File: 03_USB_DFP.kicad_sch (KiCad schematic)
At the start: 0 parts

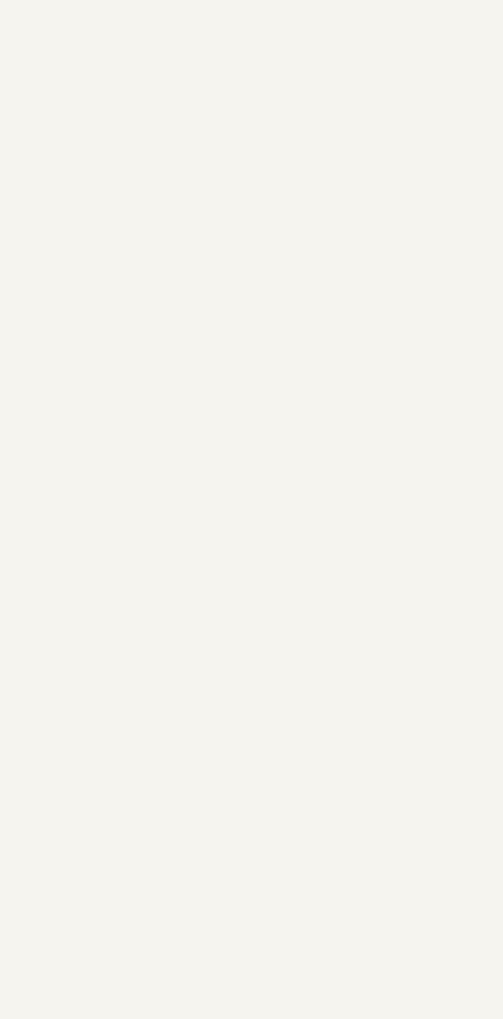
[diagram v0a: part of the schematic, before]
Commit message: add usb hub controller schematic, fix up redriver
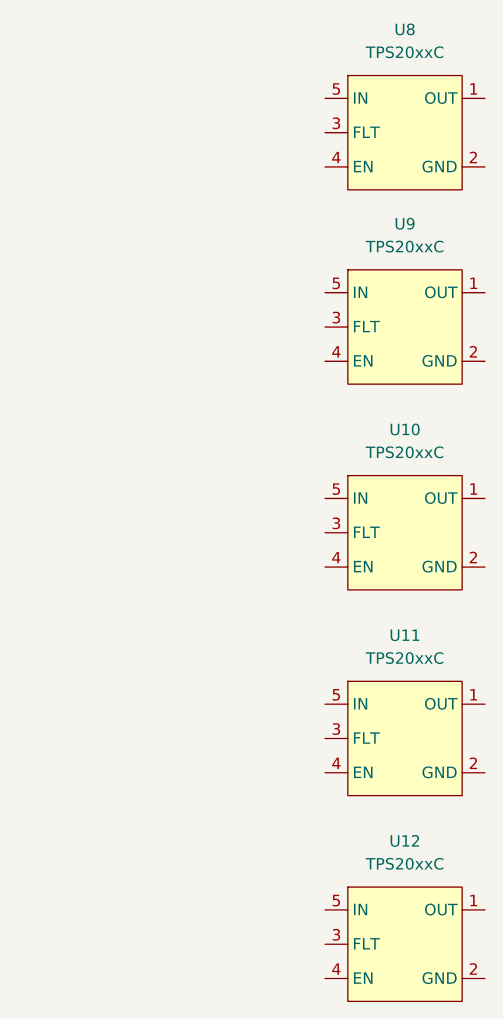
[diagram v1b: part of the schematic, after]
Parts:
- added U10, U11, U12, U8, U9: TPS20xxC, Package_TO_SOT_SMD:SOT-23-5, symbol CakeUSB:TPS20xxC
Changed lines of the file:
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@@
     (effects (font (size 1.27 1.27)) (justify left bottom))
   )
+  (symbol (lib_id "CakeUSB:TPS20xxC") (at 181.61 133.35 0) (unit 1)
+    (in_bom yes) (on_board yes) (dnp no) (fields_autoplaced)
+    (property "Reference" "U12" (at 181.61 121.92 0)
+      (effects (font (size 1.27 1.27)))
+    )
+    (property "Value" "TPS20xxC" (at 181.61 124.46 0)
+      (effects (font (size 1.27 1.27)))
+    )
+    (property "Footprint" "Package_TO_SOT_SMD:SOT-23-5" (at 203.2 114.3 0)
+      (effects (font (size 1.27 1.27)) hide)
+    )
+    (property "Datasheet" "https://www.ti.com/lit/ds/symlink/tps2001c.pdf" (at 212.09 116.84 0)
+      (effects (font (size 1.27 1.27)) hide)
+    )
+    (pin "1")
+    (pin "5")
+    (pin "2")
+    (pin "3")
+    (pin "4")
+    (instances
+      (project "USBHUB"
+        (path "/d5edc647-9ac3-4ac1-ab8a-57c77be3f4d3/aef239ad-726b-4cbb-b085-3b57a4599b3b"
+          (reference "U12") (unit 1)
+        )
+      )
+    )
+  )
+  (symbol (lib_id "CakeUSB:TPS20xxC") (at 181.61 87.63 0) (unit 1)
+    (in_bom yes) (on_board yes) (dnp no) (fields_autoplaced)
+    (property "Reference" "U10" (at 181.61 76.2 0)
+      (effects (font (size 1.27 1.27)))
+    )
+    (property "Value" "TPS20xxC" (at 181.61 78.74 0)
+      (effects (font (size 1.27 1.27)))
+    )
+    (property "Footprint" "Package_TO_SOT_SMD:SOT-23-5" (at 203.2 68.58 0)
+      (effects (font (size 1.27 1.27)) hide)
+    )
+    (property "Datasheet" "https://www.ti.com/lit/ds/symlink/tps2001c.pdf" (at 212.09 71.12 0)
+      (effects (font (size 1.27 1.27)) hide)
+    )
+    (pin "1")
+    (pin "5")
+    (pin "2")
+    (pin "3")
+    (pin "4")
+    (instances
+      (project "USBHUB"
+        (path "/d5edc647-9ac3-4ac1-ab8a-57c77be3f4d3/aef239ad-726b-4cbb-b085-3b57a4599b3b"
+          (reference "U10") (unit 1)
+        )
+      )
+    )
+  )
+  (symbol (lib_id "CakeUSB:TPS20xxC") (at 181.61 43.18 0) (unit 1)
+    (in_bom yes) (on_board yes) (dnp no) (fields_autoplaced)
+    (property "Reference" "U8" (at 181.61 31.75 0)
+      (effects (font (size 1.27 1.27)))
+    )
+    (property "Value" "TPS20xxC" (at 181.61 34.29 0)
+      (effects (font (size 1.27 1.27)))
+    )
+    (property "Footprint" "Package_TO_SOT_SMD:SOT-23-5" (at 203.2 24.13 0)
+      (effects (font (size 1.27 1.27)) hide)
+    )
+    (property "Datasheet" "https://www.ti.com/lit/ds/symlink/tps2001c.pdf" (at 212.09 26.67 0)
+      (effects (font (size 1.27 1.27)) hide)
+    )
+    (pin "1")
+    (pin "5")
+    (pin "2")
+    (pin "3")
+    (pin "4")
+    (instances
+      (project "USBHUB"
+        (path "/d5edc647-9ac3-4ac1-ab8a-57c77be3f4d3/aef239ad-726b-4cbb-b085-3b57a4599b3b"
+          (reference "U8") (unit 1)
+        )
+      )
+    )
+  )
+  (symbol (lib_id "CakeUSB:TPS20xxC") (at 181.61 64.77 0) (unit 1)
+    (in_bom yes) (on_board yes) (dnp no) (fields_autoplaced)
+    (property "Reference" "U9" (at 181.61 53.34 0)
+      (effects (font (size 1.27 1.27)))
+    )
+    (property "Value" "TPS20xxC" (at 181.61 55.88 0)
+      (effects (font (size 1.27 1.27)))
+    )
+    (property "Footprint" "Package_TO_SOT_SMD:SOT-23-5" (at 203.2 45.72 0)
+      (effects (font (size 1.27 1.27)) hide)
+    )
+    (property "Datasheet" "https://www.ti.com/lit/ds/symlink/tps2001c.pdf" (at 212.09 48.26 0)
+      (effects (font (size 1.27 1.27)) hide)
+    )
+    (pin "1")
+    (pin "5")
+    (pin "2")
+    (pin "3")
+    (pin "4")
+    (instances
+      (project "USBHUB"
+        (path "/d5edc647-9ac3-4ac1-ab8a-57c77be3f4d3/aef239ad-726b-4cbb-b085-3b57a4599b3b"
+          (reference "U9") (unit 1)
+        )
+      )
+    )
+  )
+  (symbol (lib_id "CakeUSB:TPS20xxC") (at 181.61 110.49 0) (unit 1)
+    (in_bom yes) (on_board yes) (dnp no) (fields_autoplaced)
+    (property "Reference" "U11" (at 181.61 99.06 0)
+      (effects (font (size 1.27 1.27)))
+    )
+    (property "Value" "TPS20xxC" (at 181.61 101.6 0)
+      (effects (font (size 1.27 1.27)))
+    )
+    (property "Footprint" "Package_TO_SOT_SMD:SOT-23-5" (at 203.2 91.44 0)
+      (effects (font (size 1.27 1.27)) hide)
+    )
+    (property "Datasheet" "https://www.ti.com/lit/ds/symlink/tps2001c.pdf" (at 212.09 93.98 0)
+      (effects (font (size 1.27 1.27)) hide)
+    )
+    (pin "1")
+    (pin "5")
+    (pin "2")
+    (pin "3")
+    (pin "4")
+    (instances
+      (project "USBHUB"
+        (path "/d5edc647-9ac3-4ac1-ab8a-57c77be3f4d3/aef239ad-726b-4cbb-b085-3b57a4599b3b"
+          (reference "U11") (unit 1)
+        )
+      )
+    )
+  )
 )

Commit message: WIP hub and DFP
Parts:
- added D12, D13, D14, D15, D16, D17, D18, D19, D20, D21, D22, D23: ESD122DMx, Cake_USB:ESD122DMX, symbol CakeUSB:ESD122DMx
- added U14, U15, U16, U17: USB_3_Type_A_Molex_484080003, Cake_USB:Molex_484080003, symbol CakeUSB:USB_3_Type_A_Molex_484080003
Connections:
- new net GND: D12.1 (GND), D13.1 (GND), D14.1 (GND), D15.1 (GND), D16.1 (GND), D17.1 (GND), D18.1 (GND), D19.1 (GND), D20.1 (GND), D21.1 (GND), D22.1 (GND), D23.1 (GND), U14.4 (GND), U14.7 (DRAIN), U15.4 (GND), U15.7 (DRAIN), U16.4 (GND), U16.7 (DRAIN), U17.4 (GND), U17.7 (DRAIN)
- new net HUB1_DS1_DM: D14.3 (IO2), U14.2 (D-)
- new net HUB1_DS1_DP: D14.2 (IO1), U14.3 (D+)
- new net HUB1_DS1_RXM: D13.3 (IO2), U14.5 (SSRX-)
- new net HUB1_DS1_RXP: D13.2 (IO1), U14.6 (SSRX+)
- new net HUB1_DS1_TXM: D12.3 (IO2), U14.8 (SSTX-)
- new net HUB1_DS1_TXP: D12.2 (IO1), U14.9 (SSTX+)
- new net HUB1_DS2_DM: D17.3 (IO2), U15.2 (D-)
- new net HUB1_DS2_DP: D17.2 (IO1), U15.3 (D+)
- new net HUB1_DS2_RXM: D16.3 (IO2), U15.5 (SSRX-)
- new net HUB1_DS2_RXP: D16.2 (IO1), U15.6 (SSRX+)
- new net HUB1_DS2_TXM: D15.3 (IO2), U15.8 (SSTX-)
- new net HUB1_DS2_TXP: D15.2 (IO1), U15.9 (SSTX+)
- new net HUB1_DS3_DM: D20.3 (IO2), U16.2 (D-)
- new net HUB1_DS3_DP: D20.2 (IO1), U16.3 (D+)
- new net HUB1_DS3_RXM: D19.3 (IO2), U16.5 (SSRX-)
- new net HUB1_DS3_RXP: D19.2 (IO1), U16.6 (SSRX+)
- new net HUB1_DS3_TXM: D18.3 (IO2), U16.8 (SSTX-)
- new net HUB1_DS3_TXP: D18.2 (IO1), U16.9 (SSTX+)
- new net HUB1_DS4_DM: D23.3 (IO2), U17.2 (D-)
- new net HUB1_DS4_DP: D23.2 (IO1), U17.3 (D+)
- new net HUB1_DS4_RXM: D22.3 (IO2), U17.5 (SSRX-)
- new net HUB1_DS4_RXP: D22.2 (IO1), U17.6 (SSRX+)
- new net HUB1_DS4_TXM: D21.3 (IO2), U17.8 (SSTX-)
- new net HUB1_DS4_TXP: D21.2 (IO1), U17.9 (SSTX+)
- new net USB_DS1_VBUS: U14.1 (VBUS)
- new net USB_DS2_VBUS: U15.1 (VBUS)
- new net USB_DS3_VBUS: U16.1 (VBUS)
- new net USB_DS4_VBUS: U17.1 (VBUS)
- no-connect marks 0 -> 8
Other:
- note removed: "Each output port must have ESD + power switch TPS2001C e.g."
- moved on the sheet: U10, U11, U12, U8, U9

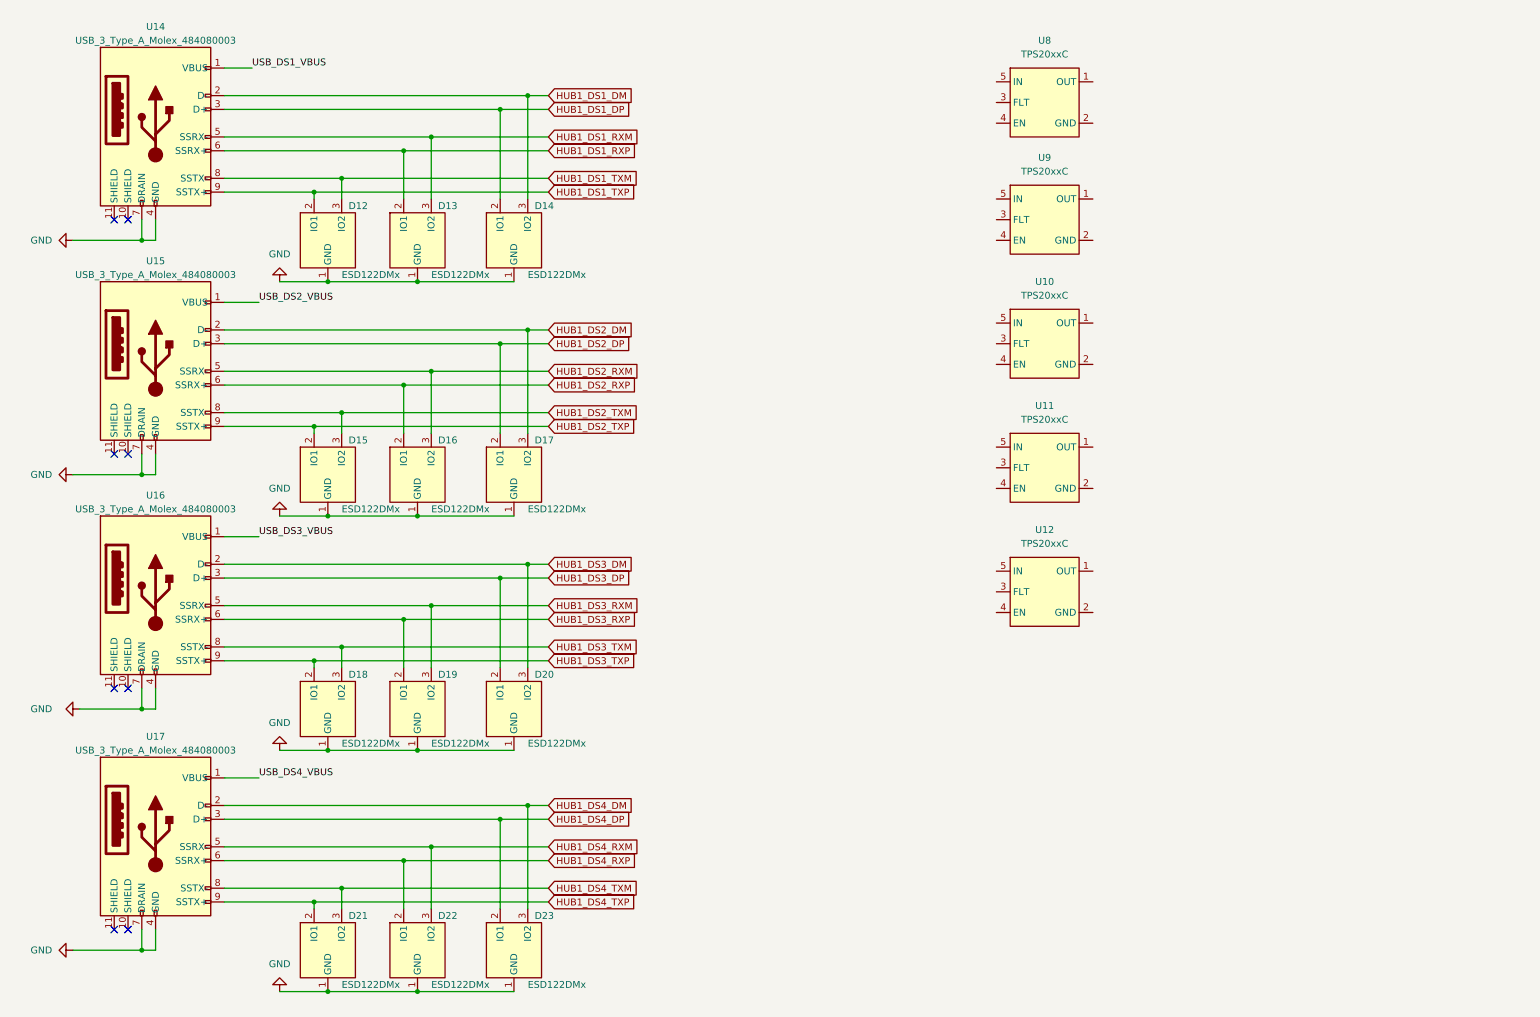
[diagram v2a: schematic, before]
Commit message: finish up schematics and ERC
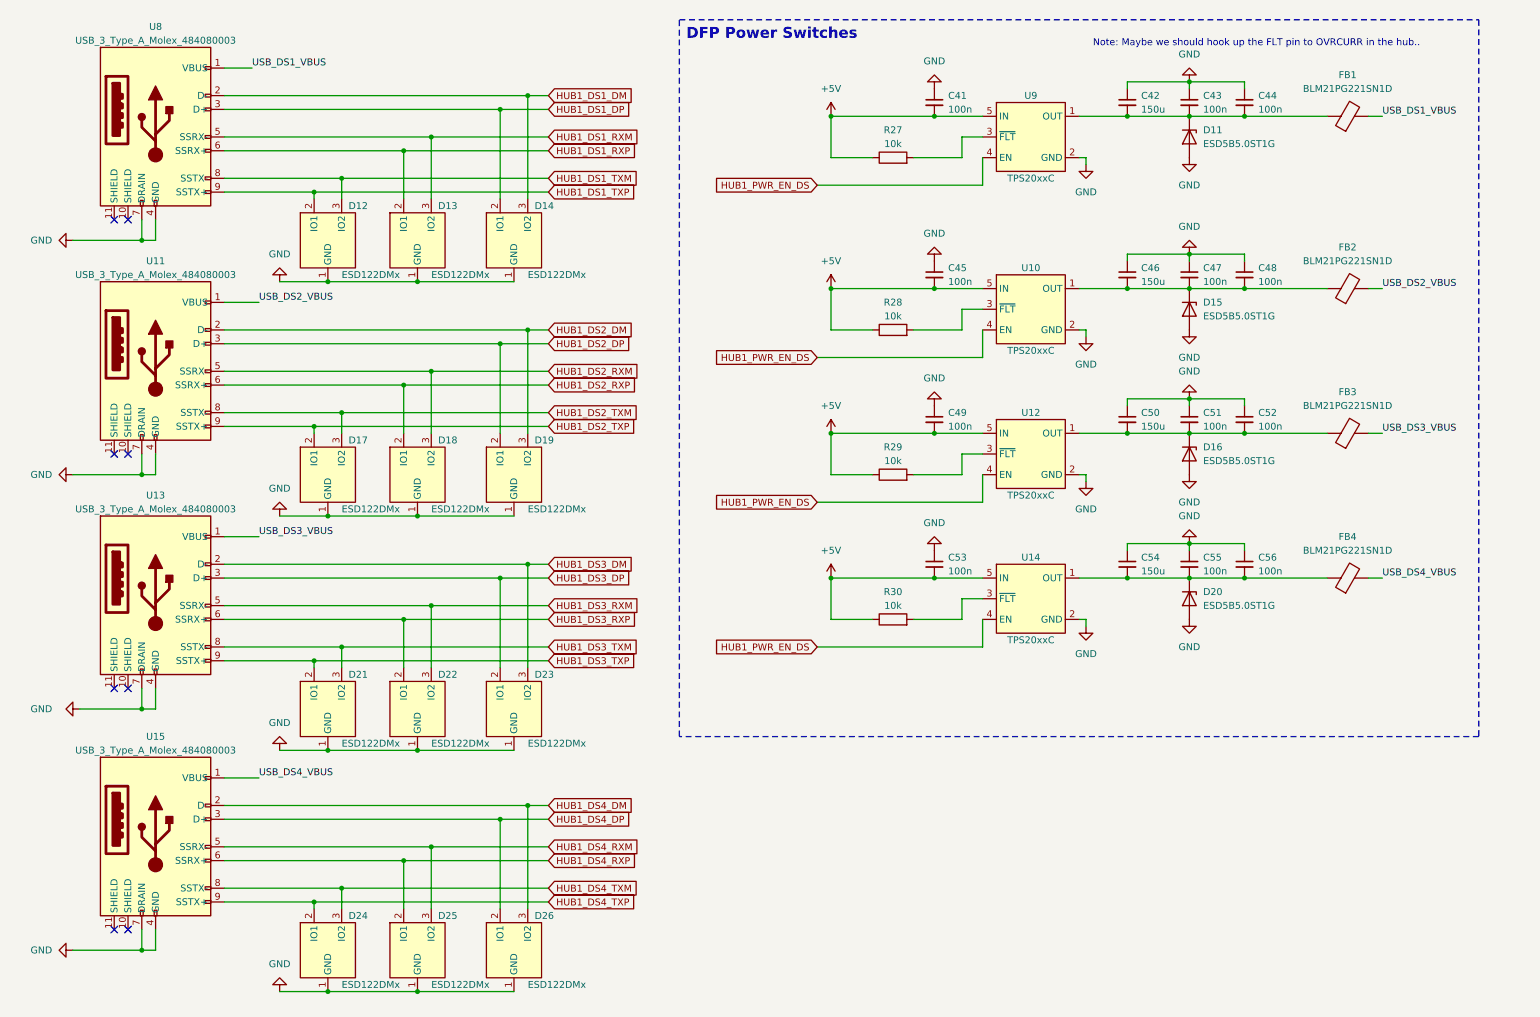
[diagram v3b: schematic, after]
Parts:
- removed U11, U9: TPS20xxC, Package_TO_SOT_SMD:SOT-23-5, symbol CakeUSB:TPS20xxC
- added C41, C43, C44, C45, C47, C48, C49, C51, C52, C53, C55, C56: 100n, symbol Device:C_Small
- added C42, C46, C50, C54: 150u, symbol Device:C_Small
- added D11, D15, D16, D20: ESD5B5.0ST1G, symbol Device:D_Zener
- added FB1, FB2, FB3, FB4: BLM21PG221SN1D, symbol Device:FerriteBead
- added R27, R28, R29, R30: 10k, symbol Device:R
- added U14: TPS20xxC, Package_TO_SOT_SMD:SOT-23-5, symbol CakeUSB:TPS20xxC
- renumbered D15 to D17, D16 to D18, D17 to D19, D18 to D21, D19 to D22, D20 to D23, D21 to D24, D22 to D25, D23 to D26, U15 to U11, U16 to U13, U17 to U15, U14 to U8, U8 to U9
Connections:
- net GND: now also U10.2 (GND), U12.2 (GND), U9.2 (GND), C41.1, C42.1, C43.1, C44.1, C45.1, C46.1, C47.1, C48.1, C49.1, C50.1, C51.1, C52.1, C53.1, C54.1, C55.1, C56.1, D11.2 (A), D15.2 (A), D16.2 (A), D20.2 (A), U14.2 (GND)
- net USB_DS1_VBUS: now also FB1.2
- net USB_DS2_VBUS: now also FB2.2
- net USB_DS3_VBUS: now also FB3.2
- net USB_DS4_VBUS: now also FB4.2
- net at U12.1 (OUT): now also C50.2, C51.2, C52.2, D16.1 (K), FB3.1
- net at U12.3 (~{FLT}): now also R29.2
- net HUB1_PWR_EN_DS: now reaches U12.4 (EN)
- net HUB1_PWR_EN_DS: now also U10.4 (EN), U9.4 (EN), U14.4 (EN)
- net +5V: now reaches U12.5 (IN)
- net +5V: now also U10.5 (IN), U9.5 (IN), C41.2, C45.2, C49.2, C53.2, R27.1, R28.1, R29.1, R30.1, U14.5 (IN)
- net at U10.1 (OUT): now also C46.2, C47.2, C48.2, D15.1 (K), FB2.1
- net at U10.3 (~{FLT}): now also R28.2
- net at U9.1 (OUT): now also C42.2, C43.2, C44.2, D11.1 (K), FB1.1
- net at U9.3 (~{FLT}): now also R27.2
- new net: C54.2, C55.2, C56.2, D20.1 (K), FB4.1, U14.1 (OUT)
- new net: R30.2, U14.3 (~{FLT})
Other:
- note added: "DFP Power Switches"
- note added: "Note: Maybe we should hook up the FLT pin to OVRCURR in the hub.."
- moved on the sheet: U9

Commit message: finish setting footprints
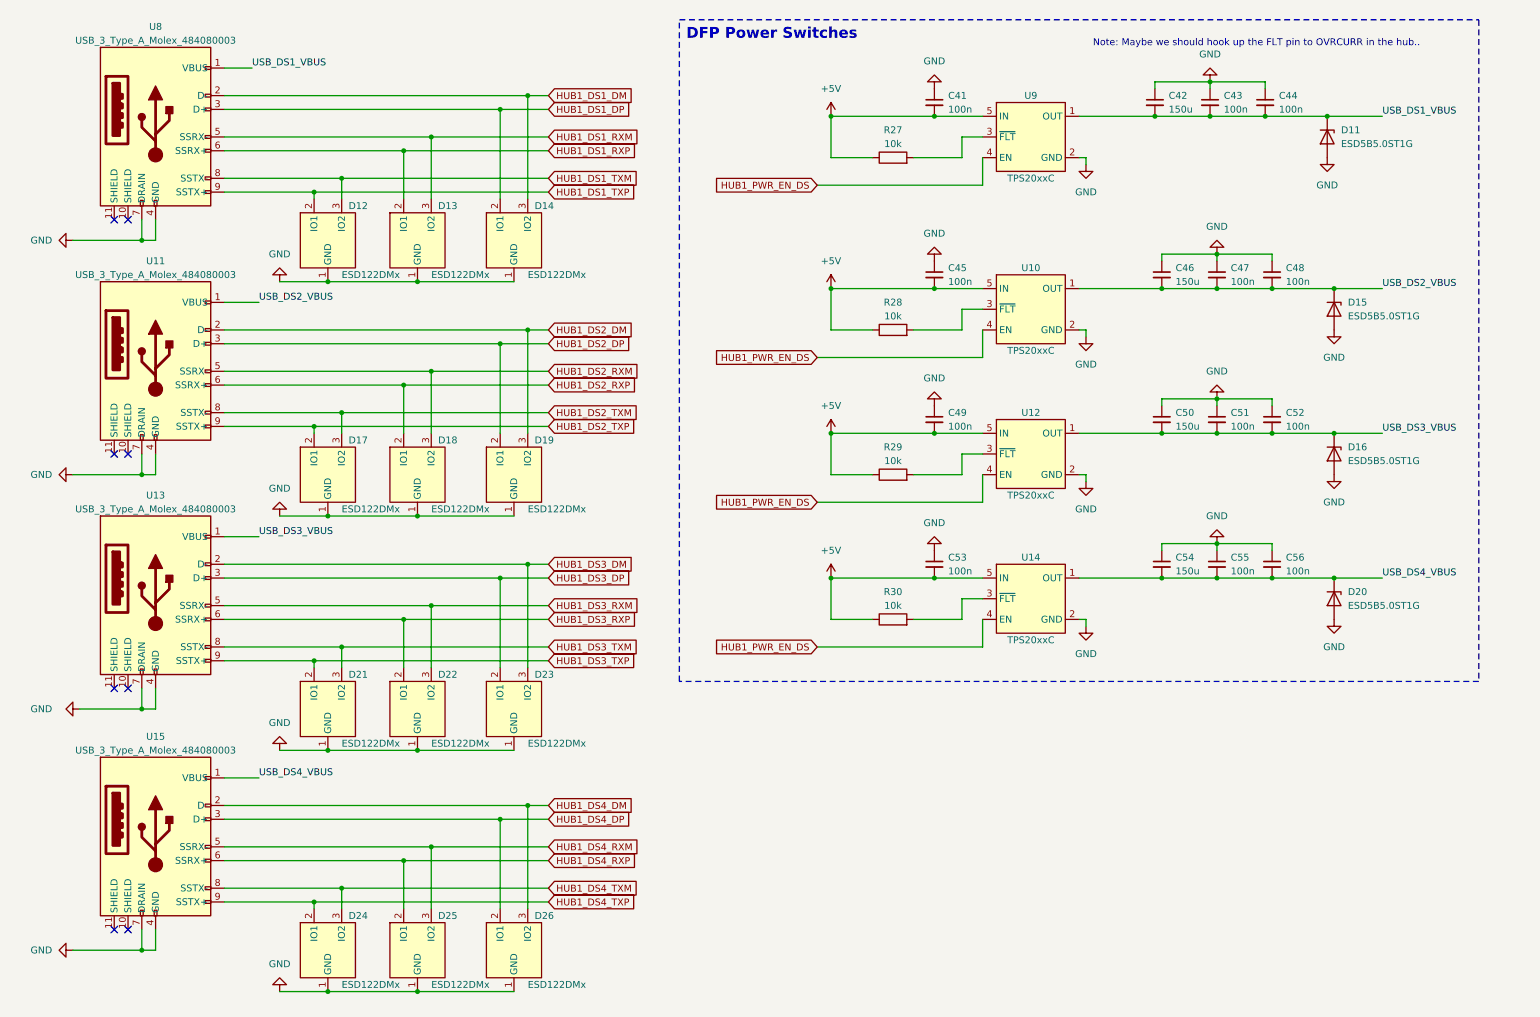
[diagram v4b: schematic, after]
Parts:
- removed FB1, FB2, FB3, FB4: BLM21PG221SN1D, symbol Device:FerriteBead
- C41, C43, C44, C45, C47, C48, C49, C51, C52, C53, C55, C56: footprint (none) -> Capacitor_SMD:C_0603_1608Metric
- C42, C46, C50, C54: footprint (none) -> Capacitor_SMD:C_Elec_6.3x7.7
- D11, D15, D16, D20: footprint (none) -> Diode_SMD:D_SOD-523
- R27, R28, R29, R30: footprint (none) -> Resistor_SMD:R_0603_1608Metric
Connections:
- net USB_DS1_VBUS: now also C42.2, C43.2, C44.2, D11.1 (K), U9.1 (OUT)
- net USB_DS2_VBUS: now also C46.2, C47.2, C48.2, D15.1 (K), U10.1 (OUT)
- net USB_DS3_VBUS: now also C50.2, C51.2, C52.2, D16.1 (K), U12.1 (OUT)
- net USB_DS4_VBUS: now also C54.2, C55.2, C56.2, D20.1 (K), U14.1 (OUT)
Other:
- moved on the sheet: C42, C43, C44, D11
